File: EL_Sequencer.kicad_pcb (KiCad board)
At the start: 2 copper layers, 95 x 130 mm, 177 parts, among them J1 B2B-PH-K-S, J10 Header_01x02_Male, J11 Header_01x02_Male, J12 Header_01x02_Male, J13 Header_01x02_Male, J14 Header_01x02_Male, J15 Header_01x02_Male, J16 Header_01x02_Male, J17 Header_01x02_Male, J18 Header_01x02_Male, J19 Header_01x02_Male, J2 Conn_01x06, J20 Header_01x02_Male, J21 Header_01x02_Male, J22 Header_01x02_Male, J23 Header_01x02_Male, J24 Header_01x02_Male, J25 Header_01x02_Male, J26 Header_01x02_Male, J27 Header_01x02_Male, J28 Header_01x02_Male, J29 Header_01x02_Male, J3 Header_01x02_Male, J4 Header_01x02_Male, J5 Conn2x5_CNC#3220-10-0100-00, J6 Header_01x02_Male, J7 Header_01x02_Male, J8 Header_01x02_Male, J9 Header_01x02_Male, Q1 Z0103NN, Q10 Z0103NN, Q11 Z0103NN, Q12 Z0103NN, Q13 Z0103NN, Q14 Z0103NN, Q15 Z0103NN, Q16 Z0103NN, Q17 Z0103NN, Q18 Z0103NN, Q19 Z0103NN, Q2 Z0103NN, Q20 Z0103NN, Q21 Z0103NN, Q22 Z0103NN, Q23 Z0103NN, Q24 Z0103NN, Q3 Z0103NN, Q4 Z0103NN, Q5 Z0103NN, Q6 Z0103NN, Q7 Z0103NN, Q8 Z0103NN, Q9 Z0103NN, SW1 FSM2JSMAA, U1 ATmega1284-AU, U10 MOC3063SM, U11 MOC3063SM, U12 MOC3063SM, U13 MOC3063SM, U14 MOC3063SM, U15 MOC3063SM, U16 MOC3063SM, U17 MOC3063SM, U18 MOC3063SM, U19 MOC3063SM, U2 NCP718BSN330T1G, U20 MOC3063SM, U21 MOC3063SM, U22 MOC3063SM, U23 MOC3063SM, U24 MOC3063SM, U25 MOC3063SM, U26 MOC3063SM, U3 MOC3063SM, U4 MOC3063SM, U5 MOC3063SM, U6 MOC3063SM, U7 MOC3063SM, U8 MOC3063SM, U9 MOC3063SM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

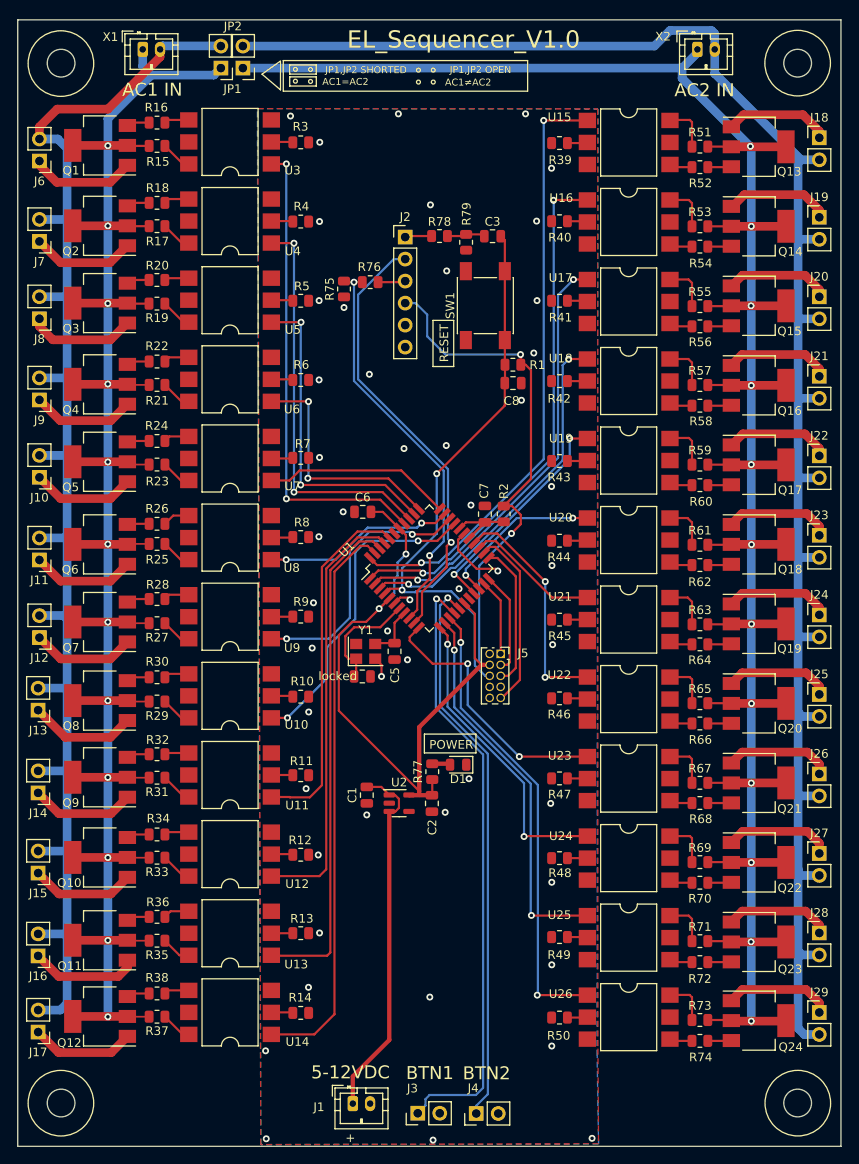
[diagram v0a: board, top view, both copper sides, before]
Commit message: Arduino compatible and smaller
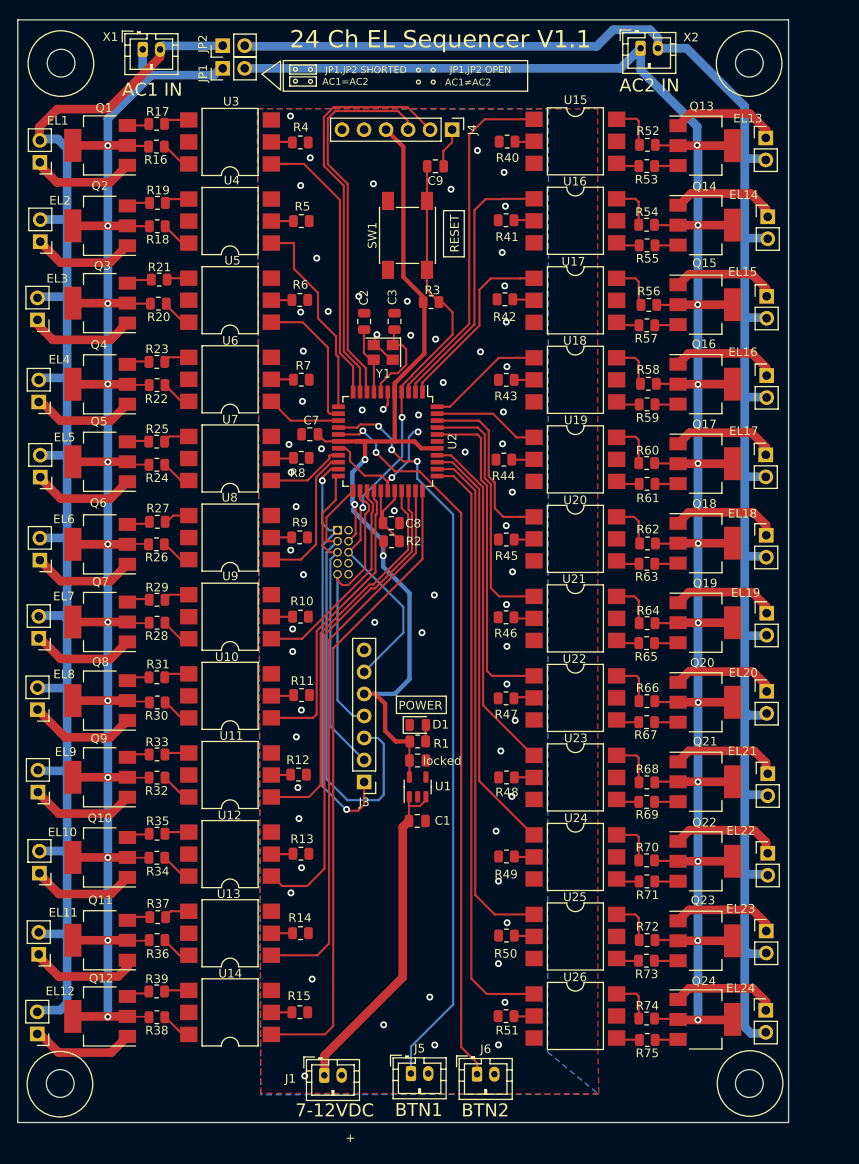
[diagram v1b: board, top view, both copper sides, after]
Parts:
- removed C5: 10pf NP0, Capacitor_SMD:C_0805_2012Metric
- removed C6: 100nf 16V, Capacitor_SMD:C_0805_2012Metric
- removed R76, R77, R78: 1k, Resistor_SMD:R_0805_2012Metric
- removed R79: 2k, Resistor_SMD:R_0805_2012Metric
- added C9: 100nf 16V, Capacitor_SMD:C_0805_2012Metric, F.Cu at (134.2, 88.3)
- added J30: Header_01x02_Male, Connector_PinHeader_2.54mm:PinHeader_1x02_P2.54mm_Vertical, F.Cu at (172.3, 185.7)
- C2: value 10uf 16V -> 10pf NP0
- C3: value 100nf 16V -> 10pf NP0
- J2: value Conn_01x06 -> Conn2x5_CNC#3220-10-0100-00; footprint Connector_PinHeader_2.54mm:PinHeader_1x06_P2.54mm_Vertical -> Connector_PinSocket_1.27mm:PinSocket_2x05_P1.27mm_Vertical; moved to B.Cu
- J3: value Header_01x02_Male -> Conn_01x07_Female; footprint Connector_PinHeader_2.54mm:PinHeader_1x02_P2.54mm_Vertical -> Connector_PinHeader_2.54mm:PinHeader_1x07_P2.54mm_Vertical
- J4: value Header_01x02_Male -> Conn_01x06; footprint Connector_PinHeader_2.54mm:PinHeader_1x02_P2.54mm_Vertical -> Connector_PinHeader_2.54mm:PinHeader_1x06_P2.54mm_Vertical
- J5: value Conn2x5_CNC#3220-10-0100-00 -> B2B-PH-K-S; footprint Connector_PinSocket_1.27mm:PinSocket_2x05_P1.27mm_Vertical -> Connector_JST:JST_PH_B2B-PH-K_1x02_P2.00mm_Vertical
- J6: value Header_01x02_Male -> B2B-PH-K-S; footprint Connector_PinHeader_2.54mm:PinHeader_1x02_P2.54mm_Vertical -> Connector_JST:JST_PH_B2B-PH-K_1x02_P2.00mm_Vertical
- R1: value 10k -> 1k
- R15, R51: value 330R -> 390R
- R3: value 390R -> 10k
- R39: value 390R -> 330R
- R75: value 2k -> 330R
- U1: value ATmega1284-AU -> NCP718BSN330T1G; footprint Package_QFP:TQFP-44_10x10mm_P0.8mm -> Package_TO_SOT_SMD:SOT-23-5
- U2: value NCP718BSN330T1G -> ATmega1284-AU; footprint Package_TO_SOT_SMD:SOT-23-5 -> Package_QFP:TQFP-44_10x10mm_P0.8mm
- locked: value 10pf NP0 -> 10uf 16V
- moved J18 137.3 mm to (88.3, 188.5), turned to 180 degrees
- moved J6 116.9 mm to (139.0, 193.1), turned to 0 degrees
- moved J4 113.6 mm to (136.1, 84.1), turned to -90 degrees
- moved R39 108.4 mm to (102.0, 183.6), turned to 180 degrees
- moved R51 102.8 mm to (142.4, 186.4)
- moved R15 101.3 mm to (118.6, 186.0)
- moved R75 93.5 mm to (158.7, 189.2), turned to 0 degrees
- moved C2 56.2 mm to (126.0, 106.2), turned to -90 degrees
- moved J5 49.5 mm to (131.4, 193.0)
- moved R1 44.8 mm to (132.2, 154.7), turned to 0 degrees
- moved U2 41.8 mm to (128.7, 120.1), turned to -90 degrees
- moved J3 38.7 mm to (126.0, 159.4), turned to 180 degrees
- moved J2 34.7 mm to (122.9, 130.3), turned to 180 degrees
- moved Y1 34.6 mm to (128.2, 109.8), turned to 180 degrees
- moved U1 25.3 mm to (132.2, 160.0), turned to 90 degrees
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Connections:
- C2 pad 2: V33 -> Net-(Y1-Pad3)
- C3 pad 1: Net-(C3-Pad1) -> Net-(Y1-Pad1)
- C3 pad 2: RESET -> GND
- C7 pad 2: AVCC -> Vo5
- C8 pad 2: RESET -> AVCC
- J18 pad 2: HV2- -> HV1-
- J2 pad 1: DTR -> TCK
- J2 pad 2: TX -> GND
- J2 pad 3: Net-(J2-Pad3) -> TDO
- J2 pad 4: V33 -> Vo5
- J2 pad 5: GND -> TMS
- J2 pad 6: GND -> RESET
- J3 pad 1: BUTTON_1 -> TCK
- J3 pad 2: GND -> TMS
- J4 pad 1: BUTTON_2 -> DTR
- J4 pad 2: GND -> TX
- J5 pad 1: TCK -> BUTTON_2
- J6 pad 1: Net-(J6-Pad1) -> BUTTON_1
- J6 pad 2: HV1- -> GND
- JP1 pad 2: HV1- -> HV2+
- JP2 pad 1: HV2+ -> HV1-
- Q1 pad 1: Net-(J6-Pad1) -> Net-(J7-Pad1)
- Q10 pad 1: Net-(J15-Pad1) -> Net-(J16-Pad1)
- Q11 pad 1: Net-(J16-Pad1) -> Net-(J17-Pad1)
- Q12 pad 1: Net-(J17-Pad1) -> Net-(J18-Pad1)
- Q13 pad 1: Net-(J18-Pad1) -> Net-(J19-Pad1)
- Q14 pad 1: Net-(J19-Pad1) -> Net-(J20-Pad1)
- Q15 pad 1: Net-(J20-Pad1) -> Net-(J21-Pad1)
- Q16 pad 1: Net-(J21-Pad1) -> Net-(J22-Pad1)
- Q17 pad 1: Net-(J22-Pad1) -> Net-(J23-Pad1)
- Q18 pad 1: Net-(J23-Pad1) -> Net-(J24-Pad1)
- Q19 pad 1: Net-(J24-Pad1) -> Net-(J25-Pad1)
- Q2 pad 1: Net-(J7-Pad1) -> Net-(J8-Pad1)
- Q20 pad 1: Net-(J25-Pad1) -> Net-(J26-Pad1)
- Q21 pad 1: Net-(J26-Pad1) -> Net-(J27-Pad1)
- Q22 pad 1: Net-(J27-Pad1) -> Net-(J28-Pad1)
- Q23 pad 1: Net-(J28-Pad1) -> Net-(J29-Pad1)
- Q24 pad 1: Net-(J29-Pad1) -> Net-(J30-Pad1)
- Q3 pad 1: Net-(J8-Pad1) -> Net-(J9-Pad1)
- Q4 pad 1: Net-(J9-Pad1) -> Net-(J10-Pad1)
- Q5 pad 1: Net-(J10-Pad1) -> Net-(J11-Pad1)
- Q6 pad 1: Net-(J11-Pad1) -> Net-(J12-Pad1)
- Q7 pad 1: Net-(J12-Pad1) -> Net-(J13-Pad1)
- Q8 pad 1: Net-(J13-Pad1) -> Net-(J14-Pad1)
- Q9 pad 1: Net-(J14-Pad1) -> Net-(J15-Pad1)
- R1 pad 1: V33 -> Vo5
- R1 pad 2: RESET -> Net-(D1-Pad2)
- R15 pad 1: Net-(R15-Pad1) -> GND
- R15 pad 2: HV1+ -> Net-(R15-Pad2)
- R16 pad 2: Net-(Q1-Pad3) -> HV1+
- R17 pad 2: HV1+ -> Net-(Q1-Pad3)
- R18 pad 2: Net-(Q2-Pad3) -> HV1+
- R19 pad 2: HV1+ -> Net-(Q2-Pad3)
- R2 pad 2: V33 -> Vo5
- R20 pad 2: Net-(Q3-Pad3) -> HV1+
- R21 pad 2: HV1+ -> Net-(Q3-Pad3)
- R22 pad 2: Net-(Q4-Pad3) -> HV1+
- R23 pad 2: HV1+ -> Net-(Q4-Pad3)
- R24 pad 2: Net-(Q5-Pad3) -> HV1+
- R25 pad 2: HV1+ -> Net-(Q5-Pad3)
- R26 pad 2: Net-(Q6-Pad3) -> HV1+
- R27 pad 2: HV1+ -> Net-(Q6-Pad3)
- R28 pad 2: Net-(Q7-Pad3) -> HV1+
- R29 pad 2: HV1+ -> Net-(Q7-Pad3)
- R3 pad 1: GND -> Vo5
- R3 pad 2: Net-(R3-Pad2) -> RESET
- R30 pad 2: Net-(Q8-Pad3) -> HV1+
- R31 pad 2: HV1+ -> Net-(Q8-Pad3)
- R32 pad 2: Net-(Q9-Pad3) -> HV1+
- R33 pad 2: HV1+ -> Net-(Q9-Pad3)
- R34 pad 2: Net-(Q10-Pad3) -> HV1+
- R35 pad 2: HV1+ -> Net-(Q10-Pad3)
- R36 pad 2: Net-(Q11-Pad3) -> HV1+
- R37 pad 2: HV1+ -> Net-(Q11-Pad3)
- R38 pad 2: Net-(Q12-Pad3) -> HV1+
- R39 pad 1: GND -> Net-(R39-Pad1)
- R39 pad 2: Net-(R39-Pad2) -> Net-(Q12-Pad3)
- R51 pad 1: Net-(R51-Pad1) -> GND
- R51 pad 2: HV2+ -> Net-(R51-Pad2)
- R52 pad 2: Net-(Q13-Pad3) -> HV2+
- R53 pad 2: HV2+ -> Net-(Q13-Pad3)
- R54 pad 2: Net-(Q14-Pad3) -> HV2+
- R55 pad 2: HV2+ -> Net-(Q14-Pad3)
- R56 pad 2: Net-(Q15-Pad3) -> HV2+
- R57 pad 2: HV2+ -> Net-(Q15-Pad3)
- R58 pad 2: Net-(Q16-Pad3) -> HV2+
- R59 pad 2: HV2+ -> Net-(Q16-Pad3)
- R60 pad 2: Net-(Q17-Pad3) -> HV2+
- R61 pad 2: HV2+ -> Net-(Q17-Pad3)
- R62 pad 2: Net-(Q18-Pad3) -> HV2+
- R63 pad 2: HV2+ -> Net-(Q18-Pad3)
- R64 pad 2: Net-(Q19-Pad3) -> HV2+
- R65 pad 2: HV2+ -> Net-(Q19-Pad3)
- R66 pad 2: Net-(Q20-Pad3) -> HV2+
- R67 pad 2: HV2+ -> Net-(Q20-Pad3)
- R68 pad 2: Net-(Q21-Pad3) -> HV2+
- R69 pad 2: HV2+ -> Net-(Q21-Pad3)
- R70 pad 2: Net-(Q22-Pad3) -> HV2+
- R71 pad 2: HV2+ -> Net-(Q22-Pad3)
- R72 pad 2: Net-(Q23-Pad3) -> HV2+
- R73 pad 2: HV2+ -> Net-(Q23-Pad3)
- R74 pad 2: Net-(Q24-Pad3) -> HV2+
- R75 pad 1: GND -> Net-(R75-Pad1)
- R75 pad 2: RX -> Net-(Q24-Pad3)
- U1 pad 1: EL_14 -> +12V
- U1 pad 2: EL_15 -> GND
- U1 pad 3: EL_16 -> +12V
- U1 pad 4: RESET -> unconnected-(U1-Pad4)
- U1 pad 5: V33 -> Vo5
- U10 pad 2: Net-(R10-Pad2) -> Net-(R11-Pad2)
- U10 pad 4: Net-(R30-Pad1) -> Net-(R31-Pad1)
- U10 pad 6: Net-(R29-Pad1) -> Net-(R30-Pad1)
- U11 pad 2: Net-(R11-Pad2) -> Net-(R12-Pad2)
- U11 pad 4: Net-(R32-Pad1) -> Net-(R33-Pad1)
- U11 pad 6: Net-(R31-Pad1) -> Net-(R32-Pad1)
- U12 pad 2: Net-(R12-Pad2) -> Net-(R13-Pad2)
- U12 pad 4: Net-(R34-Pad1) -> Net-(R35-Pad1)
- U12 pad 6: Net-(R33-Pad1) -> Net-(R34-Pad1)
- U13 pad 2: Net-(R13-Pad2) -> Net-(R14-Pad2)
- U13 pad 4: Net-(R36-Pad1) -> Net-(R37-Pad1)
- U13 pad 6: Net-(R35-Pad1) -> Net-(R36-Pad1)
- U14 pad 2: Net-(R14-Pad2) -> Net-(R15-Pad2)
- U14 pad 4: Net-(R38-Pad1) -> Net-(R39-Pad1)
- U14 pad 6: Net-(R37-Pad1) -> Net-(R38-Pad1)
- U15 pad 2: Net-(R39-Pad2) -> Net-(R40-Pad2)
- U15 pad 4: Net-(R52-Pad1) -> Net-(R53-Pad1)
- U15 pad 6: Net-(R51-Pad1) -> Net-(R52-Pad1)
- U16 pad 2: Net-(R40-Pad2) -> Net-(R41-Pad2)
- U16 pad 4: Net-(R54-Pad1) -> Net-(R55-Pad1)
- U16 pad 6: Net-(R53-Pad1) -> Net-(R54-Pad1)
- U17 pad 2: Net-(R41-Pad2) -> Net-(R42-Pad2)
- U17 pad 4: Net-(R56-Pad1) -> Net-(R57-Pad1)
- U17 pad 6: Net-(R55-Pad1) -> Net-(R56-Pad1)
- U18 pad 2: Net-(R42-Pad2) -> Net-(R43-Pad2)
- U18 pad 4: Net-(R58-Pad1) -> Net-(R59-Pad1)
- U18 pad 6: Net-(R57-Pad1) -> Net-(R58-Pad1)
- U19 pad 2: Net-(R43-Pad2) -> Net-(R44-Pad2)
- U19 pad 4: Net-(R60-Pad1) -> Net-(R61-Pad1)
- U19 pad 6: Net-(R59-Pad1) -> Net-(R60-Pad1)
- U2 pad 1: +12V -> EL_15
- U2 pad 2: GND -> EL_14
- U2 pad 3: +12V -> EL_13
- U2 pad 4: unconnected-(U2-Pad4) -> RESET
- U2 pad 5: V33 -> Vo5
- U20 pad 2: Net-(R44-Pad2) -> Net-(R45-Pad2)
- U20 pad 4: Net-(R62-Pad1) -> Net-(R63-Pad1)
- U20 pad 6: Net-(R61-Pad1) -> Net-(R62-Pad1)
- U21 pad 2: Net-(R45-Pad2) -> Net-(R46-Pad2)
- U21 pad 4: Net-(R64-Pad1) -> Net-(R65-Pad1)
- U21 pad 6: Net-(R63-Pad1) -> Net-(R64-Pad1)
- U22 pad 2: Net-(R46-Pad2) -> Net-(R47-Pad2)
- U22 pad 4: Net-(R66-Pad1) -> Net-(R67-Pad1)
- U22 pad 6: Net-(R65-Pad1) -> Net-(R66-Pad1)
- U23 pad 2: Net-(R47-Pad2) -> Net-(R48-Pad2)
- U23 pad 4: Net-(R68-Pad1) -> Net-(R69-Pad1)
- U23 pad 6: Net-(R67-Pad1) -> Net-(R68-Pad1)
- U24 pad 2: Net-(R48-Pad2) -> Net-(R49-Pad2)
- U24 pad 4: Net-(R70-Pad1) -> Net-(R71-Pad1)
- U24 pad 6: Net-(R69-Pad1) -> Net-(R70-Pad1)
- U25 pad 2: Net-(R49-Pad2) -> Net-(R50-Pad2)
- U25 pad 4: Net-(R72-Pad1) -> Net-(R73-Pad1)
- U25 pad 6: Net-(R71-Pad1) -> Net-(R72-Pad1)
- U26 pad 2: Net-(R50-Pad2) -> Net-(R51-Pad2)
- U26 pad 4: Net-(R74-Pad1) -> Net-(R75-Pad1)
- U26 pad 6: Net-(R73-Pad1) -> Net-(R74-Pad1)
- U3 pad 2: Net-(R3-Pad2) -> Net-(R4-Pad2)
- U3 pad 4: Net-(R16-Pad1) -> Net-(R17-Pad1)
- U3 pad 6: Net-(R15-Pad1) -> Net-(R16-Pad1)
- U4 pad 2: Net-(R4-Pad2) -> Net-(R5-Pad2)
- U4 pad 4: Net-(R18-Pad1) -> Net-(R19-Pad1)
- U4 pad 6: Net-(R17-Pad1) -> Net-(R18-Pad1)
- U5 pad 2: Net-(R5-Pad2) -> Net-(R6-Pad2)
- U5 pad 4: Net-(R20-Pad1) -> Net-(R21-Pad1)
- U5 pad 6: Net-(R19-Pad1) -> Net-(R20-Pad1)
- U6 pad 2: Net-(R6-Pad2) -> Net-(R7-Pad2)
- U6 pad 4: Net-(R22-Pad1) -> Net-(R23-Pad1)
- U6 pad 6: Net-(R21-Pad1) -> Net-(R22-Pad1)
- U7 pad 2: Net-(R7-Pad2) -> Net-(R8-Pad2)
- U7 pad 4: Net-(R24-Pad1) -> Net-(R25-Pad1)
- U7 pad 6: Net-(R23-Pad1) -> Net-(R24-Pad1)
- U8 pad 2: Net-(R8-Pad2) -> Net-(R9-Pad2)
- U8 pad 4: Net-(R26-Pad1) -> Net-(R27-Pad1)
- U8 pad 6: Net-(R25-Pad1) -> Net-(R26-Pad1)
- U9 pad 2: Net-(R9-Pad2) -> Net-(R10-Pad2)
- U9 pad 4: Net-(R28-Pad1) -> Net-(R29-Pad1)
- U9 pad 6: Net-(R27-Pad1) -> Net-(R28-Pad1)
- Y1 pad 1: Net-(C4-Pad1) -> Net-(Y1-Pad1)
- Y1 pad 3: Net-(C5-Pad2) -> Net-(Y1-Pad3)
- locked pad 1: Net-(C4-Pad1) -> GND
- locked pad 2: GND -> Vo5
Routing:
- net V33: track 139.6 -> 0.00 mm, vias 4 -> 0
- net Vo5: track 0.00 -> 111.0 mm, vias 0 -> 3
- net TCK: track 8.90 -> 48.8 mm, vias 0 -> 2
- net TDO: track 16.7 -> 52.6 mm
- net EL_14: track 60.8 -> 31.2 mm, vias 2 -> 0
- net EL_13: track 69.9 -> 40.8 mm, vias 2 -> 0
- net EL_15: track 50.3 -> 21.4 mm, vias 2 -> 0
- net EL_16: track 41.7 -> 13.5 mm, vias 2 -> 0
- net TMS: track 11.8 -> 36.7 mm
- net EL_1: track 55.2 -> 32.4 mm, vias 2 -> 0
- net EL_2: track 45.9 -> 23.6 mm, vias 2 -> 0
- net BUTTON_2: track 64.6 -> 86.1 mm, vias 1 -> 3
- net EL_3: track 36.7 -> 16.5 mm, vias 2 -> 0
- net EL_4: track 27.5 -> 8.66 mm, vias 2 -> 0
- net EL_23: track 44.4 -> 59.8 mm, vias 2 -> 0
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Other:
- board size 95 x 130 mm -> 89 x 127.2 mm
- board text added: "24 Ch EL Sequencer V1.1"
- board text added: "7-12VDC"
- board text added: "Corvette Engineering © 2023 24 Ch EL Sequencer V1.1 https://github.com/corvetteengineering/el_sequencer"
- board text added: "EL1"
- board text added: "EL10"
- board text added: "EL11"
- board text added: "EL12"
- board text added: "EL13"
- board text added: "EL14"
- board text added: "EL15"
- board text added: "EL16"
- board text added: "EL17"
- board text added: "EL18"
- board text added: "EL19"
- board text added: "EL2"
- board text added: "EL20"
- board text added: "EL21"
- board text added: "EL22"
- board text added: "EL23"
- board text added: "EL24"
- board text added: "EL3"
- board text added: "EL4"
- board text added: "EL5"
- board text added: "EL6"
- board text added: "EL7"
- board text added: "EL8"
- board text added: "EL9"
- board text removed: "5-12VDC"
- board text removed: "EL_Sequencer_V1.0"
